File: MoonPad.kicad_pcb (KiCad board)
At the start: 4 copper layers, 44.5 x 41.3 mm, 59 parts, among them IC1 W25Q16JVUXIQ, J1 OLED, J3 USB-C 2.0 Receptacle, SW1 Reset, U3 RP2040, U4 Hall_Sensor, U5 Hall_Sensor, U6 AP2112K-3.3, Y1 JGHC S3212000181080

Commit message: Added gerbers and drill files
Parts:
- moved C17 2.16 mm to (184.4, 105.9)
- moved R7 2.16 mm to (185.4, 105.9)
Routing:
- net Net-(U5-OUT): track 3.93 -> 1.63 mm
- net ADC_Z: track 6.38 -> 8.52 mm

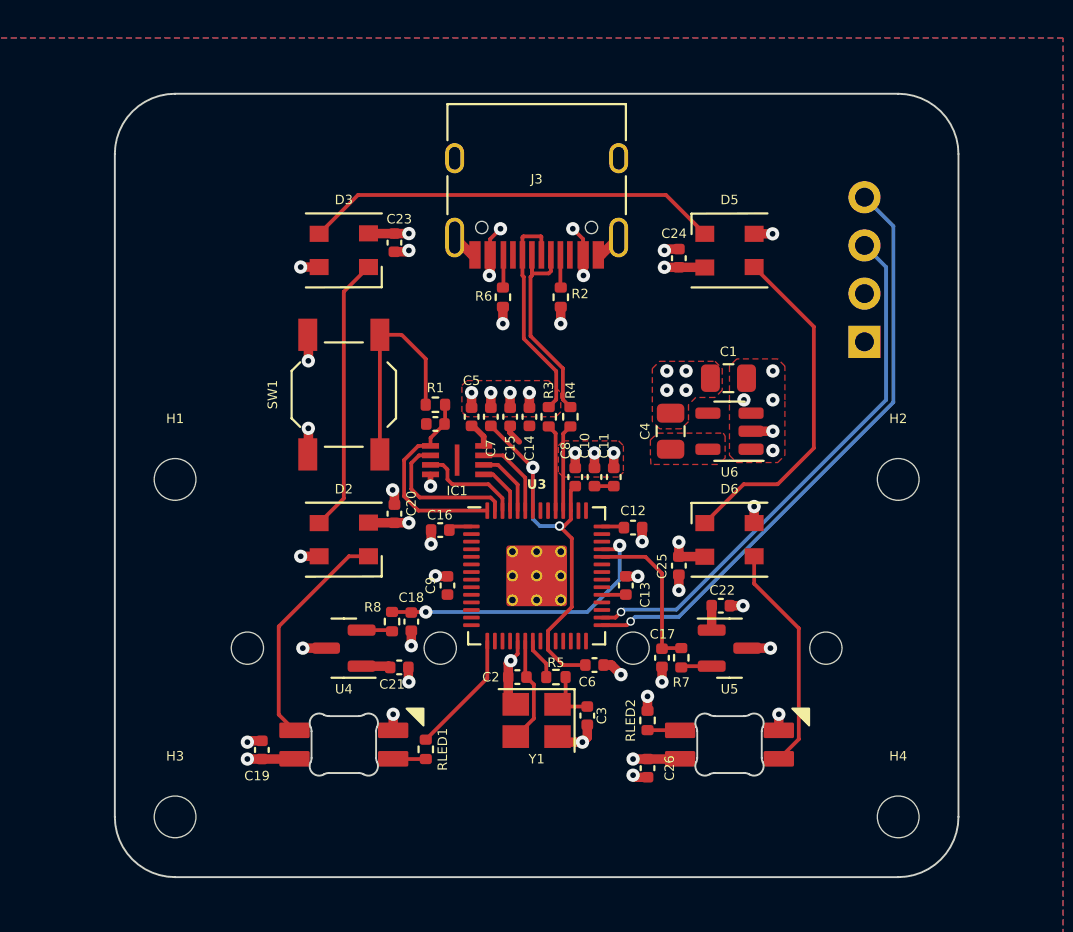
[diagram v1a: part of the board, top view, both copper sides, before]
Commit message: Migrate manufacturing files to seperate folder
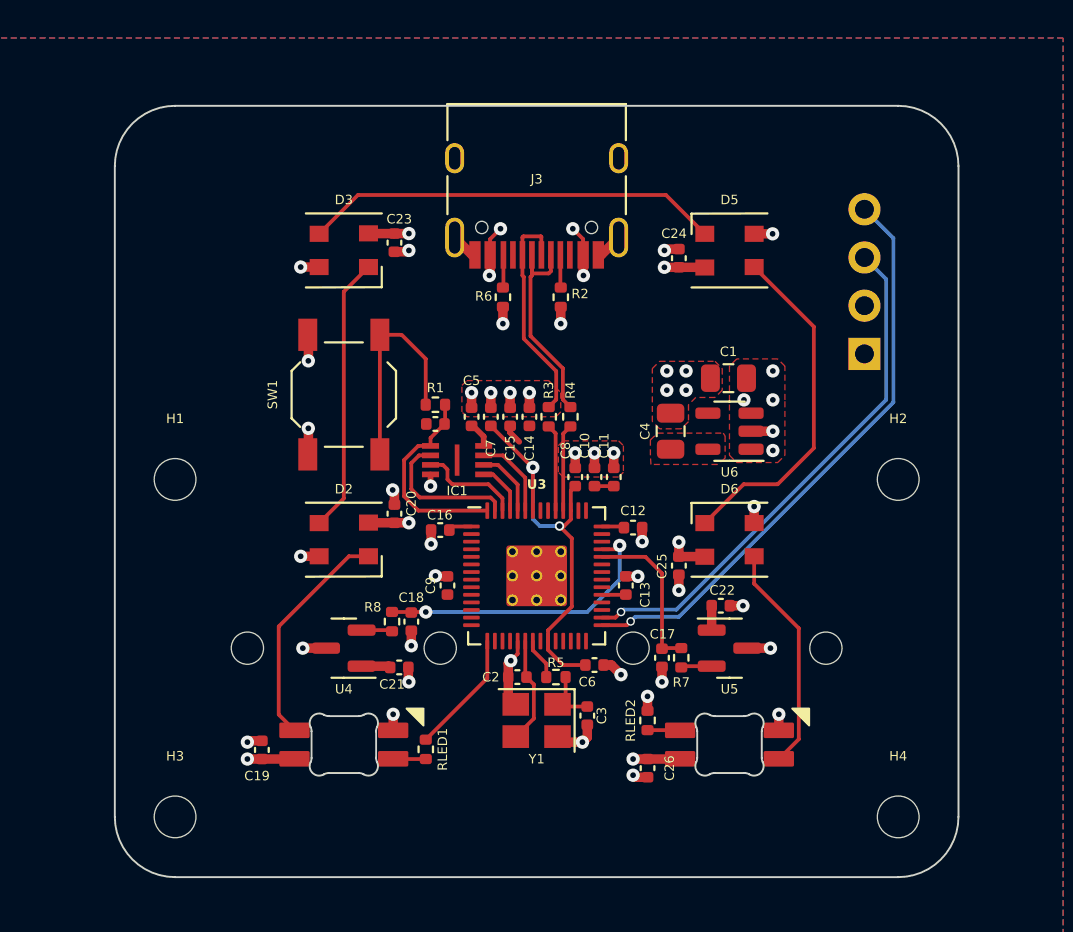
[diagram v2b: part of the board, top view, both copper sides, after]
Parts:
- moved J1 0.64 mm to (195.1, 89.9)
- moved OLED 0.64 mm to (158.8, 92.1)
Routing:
- net /OLED_SDA: track 31.7 -> 31.0 mm
- net /OLED_SCL: track 28.3 -> 27.7 mm
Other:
- board size 44.5 x 41.3 mm -> 44.5 x 40.6 mm
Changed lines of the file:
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@@
       (drillshape 0)
       (scaleselection 1)
-      (outputdirectory "")
+      (outputdirectory "Manufacturing/")
     )
   )
@@
   )
   (footprint "Moonpad:OLED 0.91" (layer "B.Cu")
-    (at 158.75 91.44)
+    (at 158.75 92.075)
     (attr through_hole)
     (fp_text reference "OLED" (at 0.87 0.504 180) (layer "B.SilkS")
@@
       (stroke (width 0.15) (type solid)) (layer "B.SilkS"))
     (model "${KIPRJMOD}/Libraries/kbd/kicad-packages3D/kbd.3dshapes/OLED-Module-with-Pins.step"
-      (offset (xyz 36.5 -6 -3.5))
+      (offset (xyz 36.5 -5.999999989 -2.86500001))
       (scale (xyz 1 1 1))
       (rotate (xyz 180 180 90))
@@
   )
   (footprint "Connector_PinHeader_2.54mm:PinHeader_1x04_P2.54mm_Vertical" (layer "B.Cu")
-    (at 195.072 89.271)
+    (at 195.072 89.906)
     (descr "Through hole straight pin header, 1x04, 2.54mm pitch, single row")
     (tags "Through hole pin header THT 1x04 2.54mm single row")
@@
   (gr_arc (start 200.025 114.3) (mid 199.095064 116.545064) (end 196.85 117.475)
     (stroke (width 0.1) (type default)) (layer "Edge.Cuts"))
-  (gr_line (start 155.575 79.375) (end 155.575 114.3)
+  (gr_line (start 155.575 80.01) (end 155.575 114.3)
     (stroke (width 0.1) (type default)) (layer "Edge.Cuts"))
   (gr_line (start 158.75 117.475) (end 196.85 117.475)
@@
   (gr_arc (start 158.75 117.475) (mid 156.504936 116.545064) (end 155.575 114.3)
     (stroke (width 0.1) (type default)) (layer "Edge.Cuts"))
-  (gr_line (start 196.85 76.2) (end 158.75 76.2)
+  (gr_line (start 196.85 76.835) (end 158.75 76.835)
     (stroke (width 0.1) (type default)) (layer "Edge.Cuts"))
-  (gr_arc (start 155.575 79.375) (mid 156.504936 77.129936) (end 158.75 76.2)
+  (gr_arc (start 155.575 80.01) (mid 156.504936 77.764936) (end 158.75 76.835)
     (stroke (width 0.1) (type default)) (layer "Edge.Cuts"))
-  (gr_arc (start 196.85 76.2) (mid 199.095064 77.129936) (end 200.025 79.375)
+  (gr_arc (start 196.85 76.835) (mid 199.095064 77.764936) (end 200.025 80.01)
     (stroke (width 0.1) (type default)) (layer "Edge.Cuts"))
-  (gr_line (start 200.025 79.375) (end 200.025 114.3)
+  (gr_line (start 200.025 80.01) (end 200.025 114.3)
     (stroke (width 0.1) (type default)) (layer "Edge.Cuts"))
   (segment (start 170.307 83.566) (end 171.069 83.566) (width 0.5) (layer "F.Cu") (net 1))
@@
   (segment (start 180.848 96.873) (end 181.864 96.873) (width 0.2) (layer "F.Cu") (net 5))
   (segment (start 182.34 99) (end 182.4 99.06) (width 0.2) (layer "F.Cu") (net 5))
-  (segment (start 170.081 106.426) (end 170.015 106.36) (width 0.5) (layer "F.Cu") (net 5))
   (segment (start 181.2375 102.6) (end 182.487 102.6) (width 0.2) (layer "F.Cu") (net 5))
   (segment (start 173.2 99.187) (end 173.26 99.127) (width 0.2) (layer "F.Cu") (net 5))
   (segment (start 187.0228 103.1748) (end 187.0228 104.4597) (width 0.5) (layer "F.Cu") (net 5))
+  (segment (start 170.015 106.36) (end 168.5775 106.36) (width 0.5) (layer "F.Cu") (net 5))
   (segment (start 174.451352 93.698) (end 174.371 93.698) (width 0.3) (layer "F.Cu") (net 5))
   (segment (start 173.2 99.187) (end 173.387 99) (width 0.2) (layer "F.Cu") (net 5))
@@
   (segment (start 176.403 93.698) (end 176.403 94.0562) (width 0.3) (layer "F.Cu") (net 5))
   (segment (start 182.487 102.6) (end 182.499 102.588) (width 0.2) (layer "F.Cu") (net 5))
-  (segment (start 170.015 106.36) (end 168.5775 106.36) (width 0.5) (layer "F.Cu") (net 5))
+  (segment (start 170.081 106.426) (end 170.015 106.36) (width 0.5) (layer "F.Cu") (net 5))
   (segment (start 179.003371 98.977451) (end 179.250207 98.977451) (width 0.2) (layer "F.Cu") (net 6))
   (segment (start 179.6 98.1625) (end 179.6 97.105) (width 0.2) (layer "F.Cu") (net 6))
   (segment (start 178.4 105.502658) (end 179.196342 106.299) (width 0.2) (layer "F.Cu") (net 6))
-  (segment (start 179.6524 99.62648) (end 179.6524 103.2428) (width 0.2) (layer "F.Cu") (net 6))
+  (segment (start 179.6524 103.220194) (end 178.4 104.472594) (width 0.2) (layer "F.Cu") (net 6))
   (segment (start 179.6 98.627658) (end 179.6 98.1625) (width 0.2) (layer "F.Cu") (net 6))
   (segment (start 177.574 95.885) (end 175.387 93.698) (width 0.2) (layer "F.Cu") (net 6))
   (segment (start 179.250207 98.977451) (end 179.6 98.627658) (width 0.2) (layer "F.Cu") (net 6))
-  (segment (start 179.003371 98.977451) (end 179.6524 99.62648) (width 0.2) (layer "F.Cu") (net 6))
   (segment (start 179.6 97.105) (end 179.832 96.873) (width 0.2) (layer "F.Cu") (net 6))
-  (segment (start 179.6524 103.2428) (end 178.4 104.4952) (width 0.2) (layer "F.Cu") (net 6))
   (segment (start 178.4 105.0375) (end 178.4 105.502658) (width 0.2) (layer "F.Cu") (net 6))
-  (segment (start 178.4 104.4952) (end 178.4 105.0375) (width 0.2) (layer "F.Cu") (net 6))
+  (segment (start 179.6524 99.62648) (end 179.6524 103.220194) (width 0.2) (layer "F.Cu") (net 6))
   (segment (start 179.196342 106.299) (end 180.368 106.299) (width 0.2) (layer "F.Cu") (net 6))
   (segment (start 177.6 95.885) (end 177.574 95.885) (width 0.2) (layer "F.Cu") (net 6))
   (segment (start 177.6 95.885) (end 177.6 98.1625) (width 0.2) (layer "F.Cu") (net 6))
+  (segment (start 178.4 104.472594) (end 178.4 105.0375) (width 0.2) (layer "F.Cu") (net 6))
+  (segment (start 179.003371 98.977451) (end 179.6524 99.62648) (width 0.2) (layer "F.Cu") (net 6))
   (via (at 177.6 95.885) (size 0.7) (drill 0.3) (layers "F.Cu" "B.Cu") (net 6))
   (via (at 179.003371 98.977451) (size 0.5) (drill 0.3) (layers "F.Cu" "B.Cu") (net 6))
@@
   (segment (start 181.95 103.8) (end 181.2375 103.8) (width 0.2) (layer "F.Cu") (net 59))
   (via (at 182.245 103.505) (size 0.45) (drill 0.3) (layers "F.Cu" "B.Cu") (net 59))
-  (segment (start 182.372 103.378) (end 185.166 103.378) (width 0.2) (layer "B.Cu") (net 59))
-  (segment (start 196.215 92.329) (end 196.215 85.334) (width 0.2) (layer "B.Cu") (net 59))
   (segment (start 182.245 103.505) (end 182.372 103.378) (width 0.2) (layer "B.Cu") (net 59))
-  (segment (start 196.215 85.334) (end 195.072 84.191) (width 0.2) (layer "B.Cu") (net 59))
   (segment (start 185.166 103.378) (end 196.215 92.329) (width 0.2) (layer "B.Cu") (net 59))
+  (segment (start 196.215 92.329) (end 196.215 85.969) (width 0.2) (layer "B.Cu") (net 59))
+  (segment (start 182.372 103.378) (end 185.166 103.378) (width 0.2) (layer "B.Cu") (net 59))
+  (segment (start 196.215 85.969) (end 195.072 84.826) (width 0.2) (layer "B.Cu") (net 59))
   (segment (start 182.753 104.002018) (end 182.555018 104.2) (width 0.2) (layer "F.Cu") (net 60))
   (segment (start 182.555018 104.2) (end 181.2375 104.2) (width 0.2) (layer "F.Cu") (net 60))
   (via (at 182.753 104.002018) (size 0.45) (drill 0.3) (layers "F.Cu" "B.Cu") (net 60))
-  (segment (start 196.596 83.175) (end 195.072 81.651) (width 0.2) (layer "B.Cu") (net 60))
-  (segment (start 182.753 104.002018) (end 182.996018 103.759) (width 0.2) (layer "B.Cu") (net 60))
   (segment (start 182.996018 103.759) (end 185.293 103.759) (width 0.2) (layer "B.Cu") (net 60))
-  (segment (start 196.596 92.456) (end 196.596 83.175) (width 0.2) (layer "B.Cu") (net 60))
+  (segment (start 182.753 104.002018) (end 182.996018 103.759) (width 0.2) (layer "B.Cu") (net 60))
+  (segment (start 196.596 92.456) (end 196.596 83.81) (width 0.2) (layer "B.Cu") (net 60))
+  (segment (start 196.596 83.81) (end 195.072 82.286) (width 0.2) (layer "B.Cu") (net 60))
   (segment (start 185.293 103.759) (end 196.596 92.456) (width 0.2) (layer "B.Cu") (net 60))
   (segment (start 167.64 86.63) (end 167.64 97.52) (width 0.2) (layer "F.Cu") (net 62))

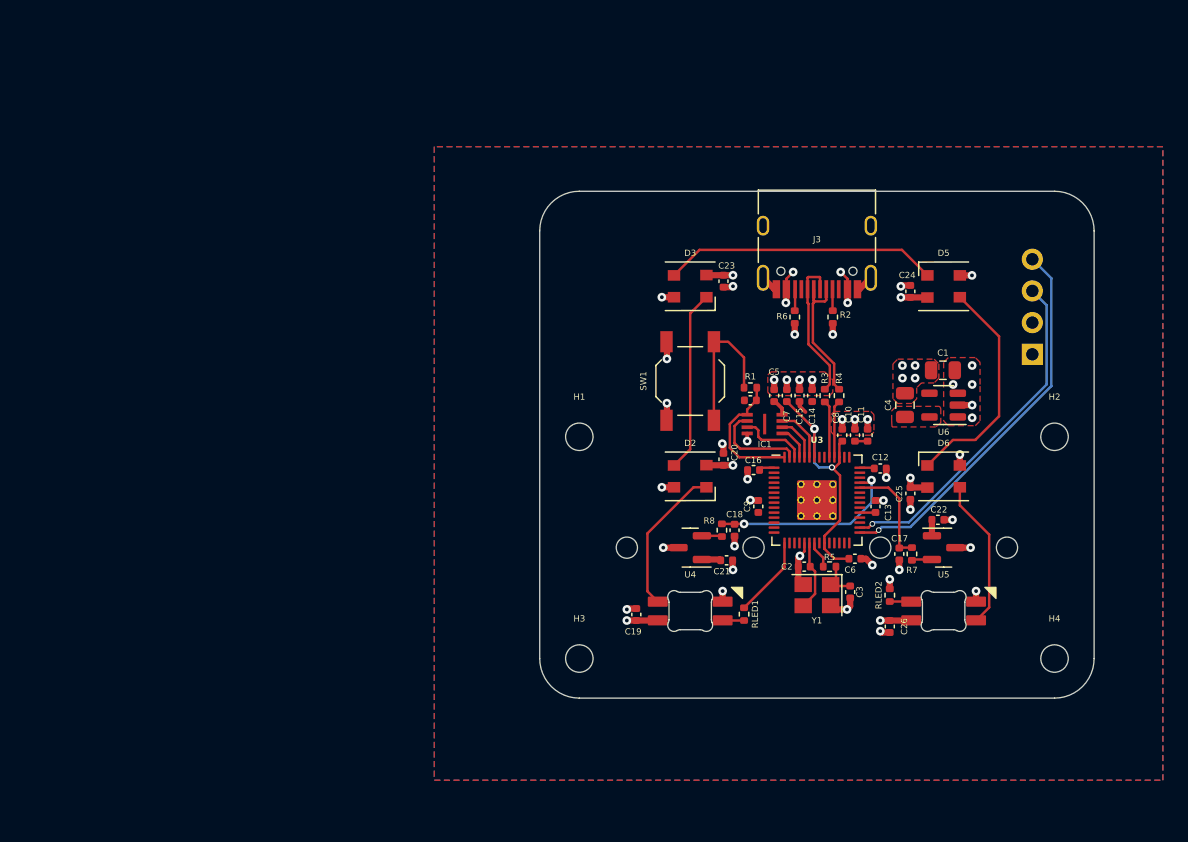
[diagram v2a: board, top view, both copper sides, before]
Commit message: Added ESD Protection
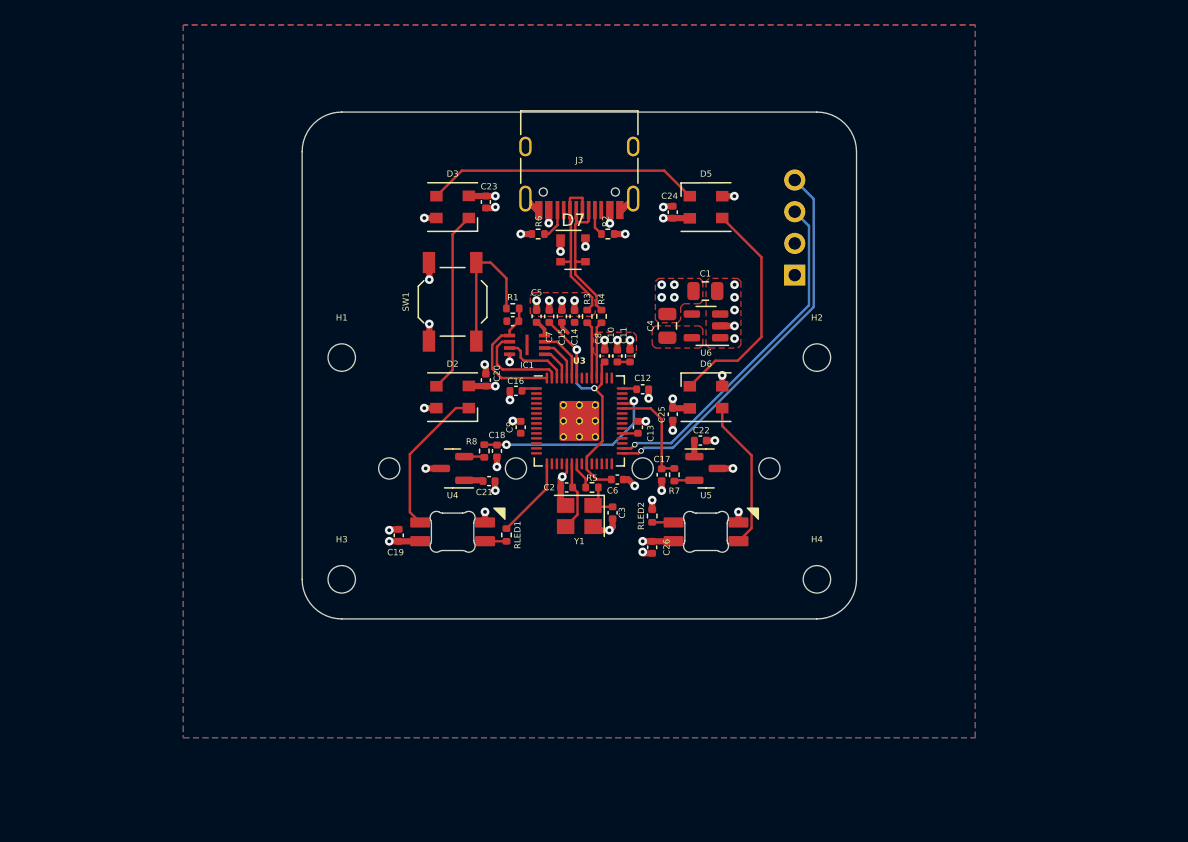
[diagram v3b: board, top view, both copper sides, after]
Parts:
- added D7: PRTR5V0U2X, Package_TO_SOT_SMD:SOT-143, F.Cu at (158.2, 81.5)
- R9: value DNF -> DNP
- moved R6 21.6 mm to (155.4, 80.3), turned to 0 degrees
- moved C14 20.1 mm to (158.4, 86.9)
- moved C18 20.1 mm to (152.1, 97.7)
- moved C19 20.1 mm to (144.3, 104.4)
- moved C21 20.1 mm to (151.5, 100.1)
- moved C22 20.1 mm to (168.5, 96.8)
- moved C24 20.1 mm to (166.2, 78.5)
- moved C5 20.1 mm to (155.3, 86.9)
- moved C6 20.1 mm to (161.8, 99.9)
- moved C7 20.1 mm to (156.3, 86.9)
- moved C9 20.1 mm to (154.1, 95.8)
- moved IC1 20.1 mm to (154.6, 89.2)
- moved J1 20.1 mm to (176.0, 83.6)
- moved OLED 20.1 mm to (139.7, 85.7)
- moved R3 20.1 mm to (159.4, 86.9)
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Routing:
- net VBUS: track 18.9 -> 16.3 mm, vias 14 -> 13
- net GND: track 41.3 -> 42.2 mm, vias 43 -> 44
- net /USB_D+: track 11.8 -> 12.7 mm
- net /USB_D-: track 11.8 -> 12.6 mm
- net Net-(J3-CC2): track 1.73 -> 2.54 mm
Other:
- board size 44.5 x 40.6 mm -> 44.4 x 40.6 mm

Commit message: Added fuse
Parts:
- added F1: Polyfuse, Fuse:Fuse_1206_3216Metric, F.Cu at (168.9, 82.5)
- moved R2 0.81 mm to (160.4, 80.8), turned to 90 degrees
- moved R6 0.81 mm to (156.1, 80.8), turned to 90 degrees
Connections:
- J3 pad A4: VBUS -> /Fuse
- J3 pad A9: VBUS -> /Fuse
- J3 pad B4: VBUS -> /Fuse
- J3 pad B9: VBUS -> /Fuse
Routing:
- net /Fuse: track 0.00 -> 15.5 mm, vias 0 -> 2
- net VBUS: track 16.3 -> 14.2 mm, vias 13 -> 11
